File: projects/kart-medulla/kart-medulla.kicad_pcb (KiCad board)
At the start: 2 copper layers, 100 x 77 mm, 59 parts, among them CN1 1990012, CN10 1990012, CN2 1990012, CN3 1990012, CN4 1990012, CN5 1990012, CN6 1990012, CN7 1990012, CN8 1990012, CN9 1990012, Q3 IRLZ44NPBF, Q4 BSS123_C5184436, U1 LM358DR, U13 MCP4922-E/SL, U14 MAX4660EUA+T, U19 L7805CDT_C20611927, U23 SSW-122-01-T-D, U24 SSW-122-01-T-S, U25 PCF8574T/3,518, U5 SN74LVC3G17DCTR

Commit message: medulla: route the valve command out at 0-10V; restore the DAC->amp copper
Schematic: one label, at (218.44, 48.26) on CN10 pin 2's stub, renamed
CMD_BRAKE__0_5V -> CMD_BRAKE__0_10V. Every connection in this chain is a label on
a stub, so nothing else moved. Netlist now splits correctly: CMD_BRAKE__0_5V =
U13.10 + U1.3, CMD_BRAKE__0_10V = CN10.2 + R19.2 + U1.1. ERC 0 violations.

PCB: CN10 pad 2's net updated, then routed to the 0-10V net on F.Cu - 45 deg from
(74.5, 90.9999) to (81.0727, 97.5726), east to (87.0, 97.5726), 0.6/0.3 via down
onto the existing B.Cu stub between U1.1 and R19.2. F.Cu because that corridor is
empty on the front layer while B.Cu is not. Clears CN10.1's through-hole pad by
~0.81 mm against a 0.254 mm rule.

Also restored: U13.10 -> U1.3, the DAC-to-amplifier copper. Six of the seven
CMD_BRAKE__0_5V segments had been deleted in KiCad, leaving that connection
unrouted; DRC flagged it as a missing connection between U1.3 and U13.10. Put the
original geometry back, since the surrounding layout was designed around it.

Zones refilled via pcbnew (kicad-cli does not refill, which is why the first DRC
run showed 6 stale-pour clearance errors). Final: DRC 0 violations, 0 unconnected.
The 5 remaining parity warnings are byte-identical to the previous commit's.
pcbnew's save rewrites the file canonically, hence the large diff; object counts
verified unchanged except the one new via.
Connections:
- CN10 pad 2: /P1/CMD_BRAKE__0_5V -> /P1/CMD_BRAKE__0_10V
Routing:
- net /P1/CMD_BRAKE__0_10V: track 2.94 -> 18.2 mm, vias 0 -> 1
- net /P1/CMD_BRAKE__0_5V: track 22.1 -> 12.4 mm
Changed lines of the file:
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@@
 			(layers "*.Cu" "*.Mask")
 			(remove_unused_layers no)
-			(net "/P1/CMD_BRAKE__0_5V")
+			(net "/P1/CMD_BRAKE__0_10V")
 			(pinfunction "2_2")
 			(pintype "passive")
@@
 	(segment
 		(start 74.5 90.9999)
-		(end 82.1099 90.9999)
-		(width 0.2)
-		(layer "B.Cu")
-		(net "/P1/CMD_BRAKE__0_5V")
-	)
-	(segment
-		(start 83.566 99.8826)
-		(end 83.566 92.456)
-		(width 0.2)
-		(layer "B.Cu")
-		(net "/P1/CMD_BRAKE__0_5V")
-	)
-	(segment
-		(start 84.6484 100.965)
-		(end 83.566 99.8826)
-		(width 0.2)
-		(layer "B.Cu")
-		(net "/P1/CMD_BRAKE__0_5V")
+		(end 81.0727 97.5726)
+		(width 0.25)
+		(layer "F.Cu")
+		(net "/P1/CMD_BRAKE__0_10V")
 	)
 	(segment
-		(start 82.1099 90.9999)
-		(end 83.566 92.456)
-		(width 0.2)
-		(layer "B.Cu")
-		(net "/P1/CMD_BRAKE__0_5V")
+		(start 81.0727 97.5726)
+		(end 87 97.5726)
+		(width 0.25)
+		(layer "F.Cu")
+		(net "/P1/CMD_BRAKE__0_10V")
 	)
-	(segment
-		(start 84.582 91.44)
-		(end 86.027 91.44)
-		(width 0.2)
-		(layer "B.Cu")
-		(net "/P1/CMD_BRAKE__0_5V")
+	(via
+		(at 87 97.5726)
+		(size 0.6)
+		(drill 0.3)
+		(layers "F.Cu" "B.Cu")
+		(net "/P1/CMD_BRAKE__0_10V")
 	)
 	(segment
-		(start 85.2551 100.965)
-		(end 84.6484 100.965)
-		(width 0.2)
+		(start 85.2551 98.425)
+		(end 86.1075 97.5726)
+		(width 0.25)
 		(layer "B.Cu")
-		(net "/P1/CMD_BRAKE__0_5V")
+		(net "/P1/CMD_BRAKE__0_10V")
 	)
 	(segment
-		(start 83.566 92.456)
-		(end 84.582 91.44)
-		(width 0.2)
+		(start 86.1075 97.5726)
+		(end 87.8449 97.5726)
+		(width 0.25)
 		(layer "B.Cu")
-		(net "/P1/CMD_BRAKE__0_5V")
+		(net "/P1/CMD_BRAKE__0_10V")
 	)
 	(segment
@@
 	)
 	(segment
-		(start 85.2551 98.425)
-		(end 86.1075 97.5726)
-		(width 0.25)
+		(start 86.027 91.44)
+		(end 84.582 91.44)
+		(width 0.2)
 		(layer "B.Cu")
-		(net "/P1/CMD_BRAKE__0_10V")
+		(net "/P1/CMD_BRAKE__0_5V")
 	)
 	(segment
-		(start 86.1075 97.5726)
-		(end 87.8449 97.5726)
-		(width 0.25)
+		(start 84.582 91.44)
+		(end 83.566 92.456)
+		(width 0.2)
 		(layer "B.Cu")
-		(net "/P1/CMD_BRAKE__0_10V")
+		(net "/P1/CMD_BRAKE__0_5V")
+	)
+	(segment
+		(start 83.566 92.456)
+		(end 83.566 99.8826)
+		(width 0.2)
+		(layer "B.Cu")
+		(net "/P1/CMD_BRAKE__0_5V")
+	)
+	(segment
+		(start 83.566 99.8826)
+		(end 84.6484 100.965)
+		(width 0.2)
+		(layer "B.Cu")
+		(net "/P1/CMD_BRAKE__0_5V")
+	)
+	(segment
+		(start 85.2551 100.965)
+		(end 84.6484 100.965)
+		(width 0.2)
+		(layer "B.Cu")
+		(net "/P1/CMD_BRAKE__0_5V")
 	)
 	(segment

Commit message: Put the design-ID QR on the board silkscreen, right of CN5
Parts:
- added REF**: kart-medulla-v2-design-id, kart-medulla:kart-medulla-v2-design-id, F.SilkS at (147.5, 51.6)

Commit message: Design-ID silkscreen: label above the QR, digits below
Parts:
- moved REF** 0.50 mm to (147.5, 51.1)
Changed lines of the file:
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@@
 	  (generator "qr_footprint.py")
 	  (layer "F.SilkS")
-	  (at 147.5 51.6)
+	  (at 147.5 51.1)
 	  (descr "Design ID 1604 0948 4608 5574 — silkscreen QR (21x21 modules at 0.45 mm) plus digits. Keep a 1.8 mm quiet zone clear of other silkscreen on all four sides.")
 	  (tags "design-id qr")
@@
 	  (fp_poly (pts (xy 2.9250 4.2750) (xy 3.3750 4.2750) (xy 3.3750 4.7250) (xy 2.9250 4.7250)) (stroke (width 0) (type solid)) (fill solid) (layer "F.SilkS"))
 	  (fp_poly (pts (xy 3.8250 4.2750) (xy 4.2750 4.2750) (xy 4.2750 4.7250) (xy 3.8250 4.7250)) (stroke (width 0) (type solid)) (fill solid) (layer "F.SilkS"))
+	  (fp_text user "Design ID" (at 0 -6.4250) (layer "F.SilkS")
+	    (effects (font (size 1.0 1.0) (thickness 0.15))))
 	  (fp_text user "1604 0948" (at 0 6.4250) (layer "F.SilkS")
 	    (effects (font (size 1.0 1.0) (thickness 0.15))))

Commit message: Silkscreen the board name kart-medulla-v2 above the design ID
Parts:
- moved REF** 2.46 mm to (145.1, 51.6)
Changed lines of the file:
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@@
 	  (generator "qr_footprint.py")
 	  (layer "F.SilkS")
-	  (at 147.5 51.1)
+	  (at 145.1 51.65)
 	  (descr "Design ID 1604 0948 4608 5574 — silkscreen QR (21x21 modules at 0.45 mm) plus digits. Keep a 1.8 mm quiet zone clear of other silkscreen on all four sides.")
 	  (tags "design-id qr")
@@
 	  (fp_poly (pts (xy 2.9250 4.2750) (xy 3.3750 4.2750) (xy 3.3750 4.7250) (xy 2.9250 4.7250)) (stroke (width 0) (type solid)) (fill solid) (layer "F.SilkS"))
 	  (fp_poly (pts (xy 3.8250 4.2750) (xy 4.2750 4.2750) (xy 4.2750 4.7250) (xy 3.8250 4.7250)) (stroke (width 0) (type solid)) (fill solid) (layer "F.SilkS"))
+	  (fp_text user "kart-medulla-v2" (at 0 -8.1250) (layer "F.SilkS")
+	    (effects (font (size 1.0 1.0) (thickness 0.15))))
 	  (fp_text user "Design ID" (at 0 -6.4250) (layer "F.SilkS")
 	    (effects (font (size 1.0 1.0) (thickness 0.15))))

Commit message: rename CMD_BRAKE -> CMD_PRES; file the MCP4922 datasheet and close two open numbers
Net rename (task item 3): CMD_BRAKE__0_5V -> CMD_PRES_DAC__0_5V and CMD_BRAKE__0_10V ->
CMD_PRES__0_10V, following the throttle channel's internal-vs-exported pattern. CMD_PRES
because it is a pressure setpoint for a proportional regulator, not a brake-force command.
Applied to schematic (4), PCB (15) and both pinout docs so the two stay in parity. ERC 0
violations, DRC 0 violations, 0 unconnected. The one remaining CMD_BRAKE is under the
'Legacy: classic ESP32' heading and correct there.

MCP4922 datasheet filed (item 4). Output swing is 0.01 V to VDD-0.04 V typical, so full
scale on the 5 V rail is ~4.96 V - 0.8% short, or 9.92 V instead of 10.00 V after the x2.
That is ~0.08 bar on a 1 bar/volt valve, negligible beside the LM358's 1-2 V of lost
headroom, so the op-amp stays the binding limit. Accuracy is only guaranteed within 1 LSb
between 10 mV and VDD-40 mV.

Two firmware constraints follow from VREF being tied to VDD, neither implemented: GA=1 for
1x gain (GA=0 asks a 5 V part for 10 V), and BUF=0 for unbuffered VREF (buffered mode's
input range stops at VDD-0.040, and VREF here is VDD).

Over-voltage number (item 2): absolute max on any output is -0.3 V to VDD+0.3 V, so -0.3 to
+5.3 V, with output current capped at 25 mA. The valve runs on 24 V, so the old CN10.2
wiring exposed VOUTB to roughly 19 V over absolute maximum with nothing in the way.

Only item 1 is left and it needs a multimeter on the assembled board.
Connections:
- net /P1/CMD_BRAKE__0_10V renamed /P1/CMD_PRES__0_10V
- net /P1/CMD_BRAKE__0_5V renamed /P1/CMD_PRES_DAC__0_5V
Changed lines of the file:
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@@
 			(layers "*.Cu" "*.Mask")
 			(remove_unused_layers no)
-			(net "/P1/CMD_BRAKE__0_10V")
+			(net "/P1/CMD_PRES__0_10V")
 			(pinfunction "2_2")
 			(pintype "passive")
@@
 			(size 0.8065 0.864)
 			(layers "B.Cu" "B.Mask")
-			(net "/P1/CMD_BRAKE__0_10V")
+			(net "/P1/CMD_PRES__0_10V")
 			(pinfunction "2_2")
 			(pintype "passive")
@@
 			(size 0.5684 1.9502)
 			(layers "B.Cu" "B.Mask" "B.Paste")
-			(net "/P1/CMD_BRAKE__0_10V")
+			(net "/P1/CMD_PRES__0_10V")
 			(pinfunction "OUT1_1")
 			(pintype "output")
@@
 			(size 0.5684 1.9502)
 			(layers "B.Cu" "B.Mask" "B.Paste")
-			(net "/P1/CMD_BRAKE__0_5V")
+			(net "/P1/CMD_PRES_DAC__0_5V")
 			(pinfunction "+IN1_3")
 			(pintype "input")
@@
 			(size 0.574 2.038)
 			(layers "B.Cu" "B.Mask" "B.Paste")
-			(net "/P1/CMD_BRAKE__0_5V")
+			(net "/P1/CMD_PRES_DAC__0_5V")
 			(pinfunction "VOUTB_10")
 			(pintype "output")
@@
 		(width 0.25)
 		(layer "F.Cu")
-		(net "/P1/CMD_BRAKE__0_10V")
+		(net "/P1/CMD_PRES__0_10V")
 	)
 	(segment
@@
 		(width 0.25)
 		(layer "F.Cu")
-		(net "/P1/CMD_BRAKE__0_10V")
+		(net "/P1/CMD_PRES__0_10V")
 	)
 	(via
@@
 		(drill 0.3)
 		(layers "F.Cu" "B.Cu")
-		(net "/P1/CMD_BRAKE__0_10V")
+		(net "/P1/CMD_PRES__0_10V")
 	)
 	(segment
@@
 		(width 0.25)
 		(layer "B.Cu")
-		(net "/P1/CMD_BRAKE__0_10V")
+		(net "/P1/CMD_PRES__0_10V")
 	)
 	(segment
@@
 		(width 0.25)
 		(layer "B.Cu")
-		(net "/P1/CMD_BRAKE__0_10V")
+		(net "/P1/CMD_PRES__0_10V")
 	)
 	(segment
@@
 		(width 0.2)
 		(layer "B.Cu")
-		(net "/P1/CMD_BRAKE__0_5V")
+		(net "/P1/CMD_PRES_DAC__0_5V")
 	)
 	(segment
@@
 		(width 0.2)
 		(layer "B.Cu")
-		(net "/P1/CMD_BRAKE__0_5V")
+		(net "/P1/CMD_PRES_DAC__0_5V")
 	)
 	(segment
@@
 		(width 0.2)
 		(layer "B.Cu")
-		(net "/P1/CMD_BRAKE__0_5V")
+		(net "/P1/CMD_PRES_DAC__0_5V")
 	)
 	(segment
@@
 		(width 0.2)
 		(layer "B.Cu")
-		(net "/P1/CMD_BRAKE__0_5V")
+		(net "/P1/CMD_PRES_DAC__0_5V")
 	)
 	(segment
@@
 		(width 0.2)
 		(layer "B.Cu")
-		(net "/P1/CMD_BRAKE__0_5V")
+		(net "/P1/CMD_PRES_DAC__0_5V")
 	)
 	(segment

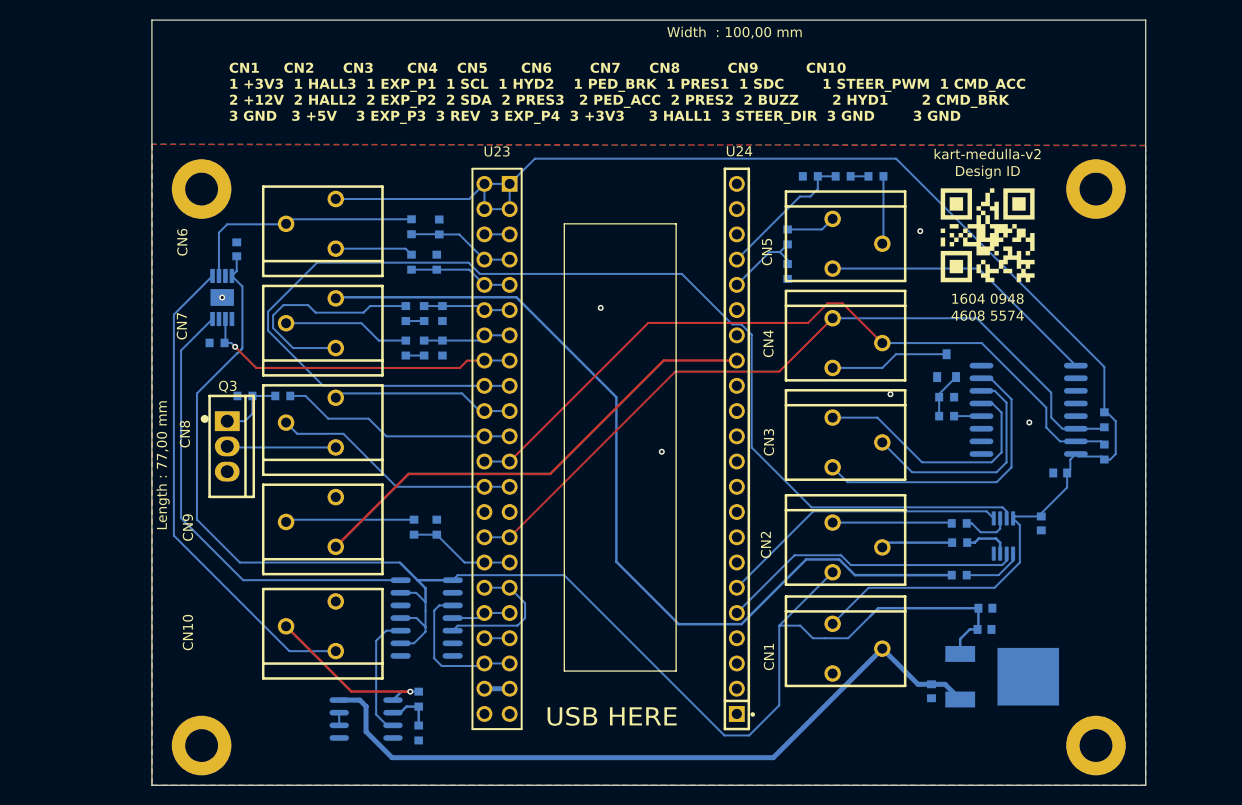
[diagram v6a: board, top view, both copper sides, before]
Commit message: placeholder 3D bodies for the WAGO connectors; KiCad has no model for them
The footprint points at TerminalBlock_WAGO.3dshapes, which does not exist in KiCad's
upstream packages3D repo at all - checked both pages of the tree via the GitLab API, it has
Altech, Ningbo-Kagnex and Phoenix terminal blocks and no WAGO. So the connectors rendered as
bare pads. Vendor models are all behind logins (3Dfindit, PARTcommunity, Ultra Librarian)
and WAGO's product page exposes no direct CAD link.

Made two VRML boxes from the footprint's own F.Fab outline - 12.00 x 12.75 mm for the
3-pole, 8.50 x 12.75 for the 2-pole - at the datasheet's 14.5 mm height. Enough to check
wire clearance and enclosure fit, which is what the 3D view is needed for. Library and board
copies both repointed to ${KIPRJMOD}/3dmodels, the same convention the Phoenix part uses.
Labelled as placeholders in README.md with the three download URLs.

The render immediately showed the ten bodies overlapping into two strips: the footprints
kept their old positions while the part grew from 2.5 mm pitch to 3.5 mm with a 12 mm body.
That is the spacing problem the re-layout has to solve, invisible until something was drawn.
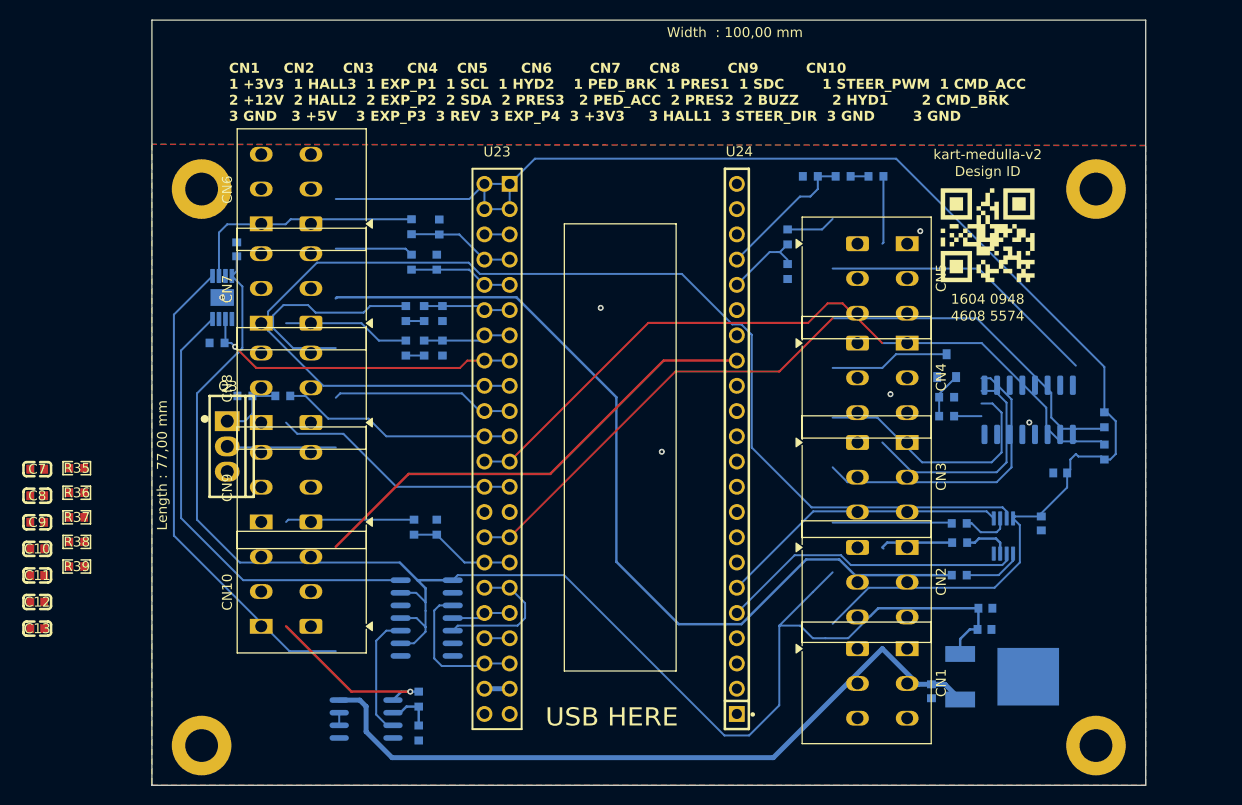
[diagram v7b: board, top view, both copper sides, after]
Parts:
- added C10: 100nF, kart-medulla:C0603, F.Cu at (49.5, 83.2)
- added C11: 100nF, kart-medulla:C0603, F.Cu at (49.5, 85.9)
- added C12: 100nF, kart-medulla:C0603, F.Cu at (49.5, 88.6)
- added C13: 100nF, kart-medulla:C0603, F.Cu at (49.5, 91.2)
- added C7: 100nF, kart-medulla:C0603, F.Cu at (49.5, 75.2)
- added C8: 100nF, kart-medulla:C0603, F.Cu at (49.5, 77.9)
- added C9: 100nF, kart-medulla:C0603, F.Cu at (49.5, 80.5)
- added R35: 10K, kart-medulla:R0603, F.Cu at (53.4, 75.1)
- added R36: 10K, kart-medulla:R0603, F.Cu at (53.4, 77.6)
- added R37: 5.1K, kart-medulla:R0603, F.Cu at (53.4, 80.0)
- added R38: 10K, kart-medulla:R0603, F.Cu at (53.4, 82.5)
- added R39: 1K, kart-medulla:R0603, F.Cu at (53.4, 85.0)
- CN1, CN10, CN2, CN3, CN4, CN5, CN6, CN7, CN8, CN9: value 1990012 -> 2601-3103; footprint kart-medulla:CONN-TH_3P-P2.50-S5.00_1990012 -> TerminalBlock_WAGO:TerminalBlock_WAGO_2601-3103_1x03_P3.50mm_Vertical
- R19: value 1K -> 2K
- REF**: moved to F.Cu
- U25: footprint kart-medulla:SOIC-16_L10.3-W7.5-P1.27-LS10.3-BL -> Package_SO:SOIC-16_3.9x9.9mm_P1.27mm
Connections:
- U1 pad 5: GND -> /P1/CMD_ACC_ESP32__0_5V
- U1 pad 6: Net-(U1B--IN2) -> /P1/ACC_AMP_FB
- U1 pad 7: Net-(U1B--IN2) -> /P1/ACC_AMP_OUT
- U13 pad 1: +5V_REG -> +3V3
- U13 pad 11: +5V_REG -> +3V3
- U13 pad 13: +5V_REG -> +3V3
- U13 pad 9: +5V_REG -> +3V3
- U14 pad 8: /P1/CMD_ACC_ESP32__0_5V -> /P1/CMD_ACC_BUF__0_5V
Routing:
- net Net-(U1B--IN2): track 1.27 -> 0.00 mm
- net (no net): track 0.00 -> 1.27 mm

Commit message: rename the DAC-output nets to say 3V3, and fix the docs that still said 0-5 V
Commit 16a35fb moved the MCP4922 U13 from +5V to +3V3 (SPI threshold fix, DS22250A p7) and
raised the LM358 U1A gain from 2 to 3 (R19 1K -> 2K) to keep ~10 V at CN10.2. It did not
update the names and prose downstream that still described the DAC outputs as 0-5 V.

Nets renamed in both the schematic and the PCB:
  CMD_PRES_DAC__0_5V  -> CMD_PRES_DAC__0_3V3
  CMD_ACC_ESP32__0_5V -> CMD_ACC_ESP32__0_3V3

CMD_ACC__0_5V is deliberately unchanged. It is the MAX4660 mux output and carries either the
DAC branch (0-3.3 V) or the driver's pedal (0-5 V), so 0-5 V is its real range.

docs/pinout-esp32-s3.md: the MCP4922 pin table still had VDD, SHDN, VREFA and VREFB on 5 V,
and described VOUTB as "0-5 V at the DAC pin ... amplifies it x2". Now +3V3 and x3, with the
open issue recorded that VOUTA has no gain stage and reaches only ~66% of the motor
controller's 0-5 V input.

parts.md and requirements.md: "LM358 x2 stage" and "MCP4922 DAC (0-5 V)" corrected, with the
resistor values named.

history.md records why R19 reads 2K in the schematic while the fabricated v1 board has 1K
fitted, since that mismatch reads as a regression and is not one.

Also included: in-progress schematic work already in the tree - the throttle buffer stage
(ACC_AMP_OUT / ACC_AMP_FB / CMD_ACC_BUF__0_5V) and the PRESSURE_1/2/3__0_3V3 renames.

ERC 0 violations.
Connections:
- net /P1/CMD_ACC_ESP32__0_5V renamed /P1/CMD_ACC_ESP32__0_3V3
- net /P1/CMD_PRES_DAC__0_5V renamed /P1/CMD_PRES_DAC__0_3V3
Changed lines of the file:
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@@
 			(size 0.5684 1.9502)
 			(layers "B.Cu" "B.Mask" "B.Paste")
-			(net "/P1/CMD_PRES_DAC__0_5V")
+			(net "/P1/CMD_PRES_DAC__0_3V3")
 			(pinfunction "+IN1_3")
 			(pintype "input")
@@
 			(size 0.5684 1.9502)
 			(layers "B.Cu" "B.Mask" "B.Paste")
-			(net "/P1/CMD_ACC_ESP32__0_5V")
+			(net "/P1/CMD_ACC_ESP32__0_3V3")
 			(pinfunction "+IN2_5")
 			(pintype "input")
@@
 			(size 0.574 2.038)
 			(layers "B.Cu" "B.Mask" "B.Paste")
-			(net "/P1/CMD_PRES_DAC__0_5V")
+			(net "/P1/CMD_PRES_DAC__0_3V3")
 			(pinfunction "VOUTB_10")
 			(pintype "output")
@@
 			(size 0.574 2.038)
 			(layers "B.Cu" "B.Mask" "B.Paste")
-			(net "/P1/CMD_ACC_ESP32__0_5V")
+			(net "/P1/CMD_ACC_ESP32__0_3V3")
 			(pinfunction "VOUTA_14")
 			(pintype "output")
@@
 		(width 0.2)
 		(layer "B.Cu")
-		(net "/P1/CMD_ACC_ESP32__0_5V")
+		(net "/P1/CMD_ACC_ESP32__0_3V3")
 	)
 	(segment
@@
 		(width 0.2)
 		(layer "B.Cu")
-		(net "/P1/CMD_ACC_ESP32__0_5V")
+		(net "/P1/CMD_ACC_ESP32__0_3V3")
 	)
 	(segment
@@
 		(width 0.2)
 		(layer "B.Cu")
-		(net "/P1/CMD_ACC_ESP32__0_5V")
+		(net "/P1/CMD_ACC_ESP32__0_3V3")
 	)
 	(segment
@@
 		(width 0.2)
 		(layer "B.Cu")
-		(net "/P1/CMD_ACC_ESP32__0_5V")
+		(net "/P1/CMD_ACC_ESP32__0_3V3")
 	)
 	(segment
@@
 		(width 0.2)
 		(layer "B.Cu")
-		(net "/P1/CMD_PRES_DAC__0_5V")
+		(net "/P1/CMD_PRES_DAC__0_3V3")
 	)
 	(segment
@@
 		(width 0.2)
 		(layer "B.Cu")
-		(net "/P1/CMD_PRES_DAC__0_5V")
+		(net "/P1/CMD_PRES_DAC__0_3V3")
 	)
 	(segment
@@
 		(width 0.2)
 		(layer "B.Cu")
-		(net "/P1/CMD_PRES_DAC__0_5V")
+		(net "/P1/CMD_PRES_DAC__0_3V3")
 	)
 	(segment
@@
 		(width 0.2)
 		(layer "B.Cu")
-		(net "/P1/CMD_PRES_DAC__0_5V")
+		(net "/P1/CMD_PRES_DAC__0_3V3")
 	)
 	(segment
@@
 		(width 0.2)
 		(layer "B.Cu")
-		(net "/P1/CMD_PRES_DAC__0_5V")
+		(net "/P1/CMD_PRES_DAC__0_3V3")
 	)
 	(zone
